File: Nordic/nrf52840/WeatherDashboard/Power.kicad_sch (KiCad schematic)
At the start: 4 parts, among them J1 Conn_01x02_Pin, U1 MPM3805GQB-33-Z

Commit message: pcie connector
Add connectins to the pcie connector
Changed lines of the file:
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@@
+	)
+	(junction
+		(at 156.21 87.63)
+		(diameter 0)
+		(color 0 0 0 0)
 	)
 	(junction
@@
 	(wire
 		(pts
+			(xy 156.21 87.63) (xy 165.1 87.63)
+		)
+		(stroke
+			(width 0)
+			(type default)
+		)
+	)
+	(wire
+		(pts
 			(xy 148.59 95.25) (xy 151.13 95.25)
 		)
@@
 		(effects
 			(font
+				(size 1.27 1.27)
+			)
+			(justify left)
+		)
+	)
+	(hierarchical_label "GND"
+		(shape input)
+		(at 165.1 87.63 0)
+		(effects
+			(font

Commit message: Layout
layout update
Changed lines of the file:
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@@
 	)
 	(junction
-		(at 120.65 87.63)
+		(at 167.64 97.79)
+		(diameter 0)
+		(color 0 0 0 0)
+	)
+	(junction
+		(at 129.54 87.63)
 		(diameter 0)
 		(color 0 0 0 0)
@@
 	(wire
 		(pts
-			(xy 156.21 97.79) (xy 170.18 97.79)
+			(xy 156.21 97.79) (xy 167.64 97.79)
 		)
 		(stroke
@@
 	(wire
 		(pts
-			(xy 129.54 85.09) (xy 120.65 85.09)
-		)
-		(stroke
-			(width 0)
-			(type default)
-		)
-	)
-	(wire
-		(pts
 			(xy 120.65 105.41) (xy 120.65 107.95)
 		)
@@
 	(wire
 		(pts
-			(xy 120.65 87.63) (xy 129.54 87.63)
+			(xy 167.64 97.79) (xy 170.18 97.79)
 		)
 		(stroke
@@
 	(wire
 		(pts
+			(xy 121.92 87.63) (xy 129.54 87.63)
+		)
+		(stroke
+			(width 0)
+			(type default)
+		)
+	)
+	(wire
+		(pts
+			(xy 121.92 88.9) (xy 121.92 87.63)
+		)
+		(stroke
+			(width 0)
+			(type default)
+		)
+	)
+	(wire
+		(pts
 			(xy 120.65 97.79) (xy 129.54 97.79)
 		)
@@
 	(wire
 		(pts
-			(xy 120.65 85.09) (xy 120.65 87.63)
+			(xy 129.54 85.09) (xy 129.54 87.63)
 		)
 		(stroke
@@
 			)
 			(justify left)
+		)
+	)
+	(symbol
+		(lib_id "power:GND")
+		(at 121.92 88.9 0)
+		(unit 1)
+		(exclude_from_sim no)
+		(in_bom yes)
+		(on_board yes)
+		(dnp no)
+		(fields_autoplaced yes)
+		(property "Reference" "#PWR018"
+			(at 121.92 95.25 0)
+			(effects
+				(font
+					(size 1.27 1.27)
+				)
+				(hide yes)
+			)
+		)
+		(property "Value" "GND"
+			(at 121.92 93.98 0)
+			(effects
+				(font
+					(size 1.27 1.27)
+				)
+			)
+		)
+		(property "Footprint" ""
+			(at 121.92 88.9 0)
+			(effects
+				(font
+					(size 1.27 1.27)
+				)
+				(hide yes)
+			)
+		)
+		(property "Datasheet" ""
+			(at 121.92 88.9 0)
+			(effects
+				(font
+					(size 1.27 1.27)
+				)
+				(hide yes)
+			)
+		)
+		(property "Description" "Power symbol creates a global label with name \"GND\" , ground"
+			(at 121.92 88.9 0)
+			(effects
+				(font
+					(size 1.27 1.27)
+				)
+				(hide yes)
+			)
+		)
+		(pin "1"
+		)
+		(instances
+			(project "WeatherDashboard"
+				(path "/189808bb-364f-4c11-a922-cc9d9f33a674/3f611b1e-4b9e-472b-bbce-6aa18c3c2d69"
+					(reference "#PWR018")
+					(unit 1)
+				)
+			)
 		)
 	)
@@
 		(on_board yes)
 		(dnp no)
-		(property "Reference" "#PWR?"
+		(property "Reference" "#PWR0102"
 			(at 156.21 93.98 0)
 			(effects
@@
 			(project "WeatherDashboard"
 				(path "/189808bb-364f-4c11-a922-cc9d9f33a674/3f611b1e-4b9e-472b-bbce-6aa18c3c2d69"
-					(reference "#PWR?")
+					(reference "#PWR0102")
 					(unit 1)
 				)
@@
 	)
 	(symbol
+		(lib_id "power:PWR_FLAG")
+		(at 167.64 97.79 0)
+		(unit 1)
+		(exclude_from_sim no)
+		(in_bom yes)
+		(on_board yes)
+		(dnp no)
+		(fields_autoplaced yes)
+		(property "Reference" "#FLG01"
+			(at 167.64 95.885 0)
+			(effects
+				(font
+					(size 1.27 1.27)
+				)
+				(hide yes)
+			)
+		)
+		(property "Value" "PWR_FLAG"
+			(at 167.64 92.71 0)
+			(effects
+				(font
+					(size 1.27 1.27)
+				)
+			)
+		)
+		(property "Footprint" ""
+			(at 167.64 97.79 0)
+			(effects
+				(font
+					(size 1.27 1.27)
+				)
+				(hide yes)
+			)
+		)
+		(property "Datasheet" "~"
+			(at 167.64 97.79 0)
+			(effects
+				(font
+					(size 1.27 1.27)
+				)
+				(hide yes)
+			)
+		)
+		(property "Description" "Special symbol for telling ERC where power comes from"
+			(at 167.64 97.79 0)
+			(effects
+				(font
+					(size 1.27 1.27)
+				)
+				(hide yes)
+			)
+		)
+		(pin "1"
+		)
+		(instances
+			(project "WeatherDashboard"
+				(path "/189808bb-364f-4c11-a922-cc9d9f33a674/3f611b1e-4b9e-472b-bbce-6aa18c3c2d69"
+					(reference "#FLG01")
+					(unit 1)
+				)
+			)
+		)
+	)
+	(symbol
 		(lib_id "power:GND")
 		(at 167.64 102.87 0)
@@
 	)
 	(symbol
-		(lib_id "power:GND")
-		(at 120.65 87.63 0)
-		(unit 1)
-		(exclude_from_sim no)
-		(in_bom yes)
-		(on_board yes)
-		(dnp no)
-		(fields_autoplaced yes)
-		(property "Reference" "#PWR01"
-			(at 120.65 93.98 0)
-			(effects
-				(font
-					(size 1.27 1.27)
-				)
-				(hide yes)
-			)
-		)
-		(property "Value" "GND"
-			(at 120.65 92.71 0)
-			(effects
-				(font
-					(size 1.27 1.27)
-				)
-			)
-		)
-		(property "Footprint" ""
-			(at 120.65 87.63 0)
-			(effects
-				(font
-					(size 1.27 1.27)
-				)
-				(hide yes)
-			)
-		)
-		(property "Datasheet" ""
-			(at 120.65 87.63 0)
-			(effects
-				(font
-					(size 1.27 1.27)
-				)
-				(hide yes)
-			)
-		)
-		(property "Description" "Power symbol creates a global label with name \"GND\" , ground"
-			(at 120.65 87.63 0)
-			(effects
-				(font
-					(size 1.27 1.27)
-				)
-				(hide yes)
-			)
-		)
-		(pin "1"
-		)
-		(instances
-			(project "WeatherDashboard"
-				(path "/189808bb-364f-4c11-a922-cc9d9f33a674/3f611b1e-4b9e-472b-bbce-6aa18c3c2d69"
-					(reference "#PWR01")
-					(unit 1)
-				)
-			)
-		)
-	)
-	(symbol
 		(lib_id "Connector:Conn_01x02_Pin")
 		(at 175.26 100.33 180)
@@
 		(dnp no)
 		(fields_autoplaced yes)
-		(property "Reference" "#PWR?"
+		(property "Reference" "#PWR0101"
 			(at 153.67 114.3 0)
 			(effects
@@
 			(project "WeatherDashboard"
 				(path "/189808bb-364f-4c11-a922-cc9d9f33a674/3f611b1e-4b9e-472b-bbce-6aa18c3c2d69"
-					(reference "#PWR?")
+					(reference "#PWR0101")
 					(unit 1)
 				)

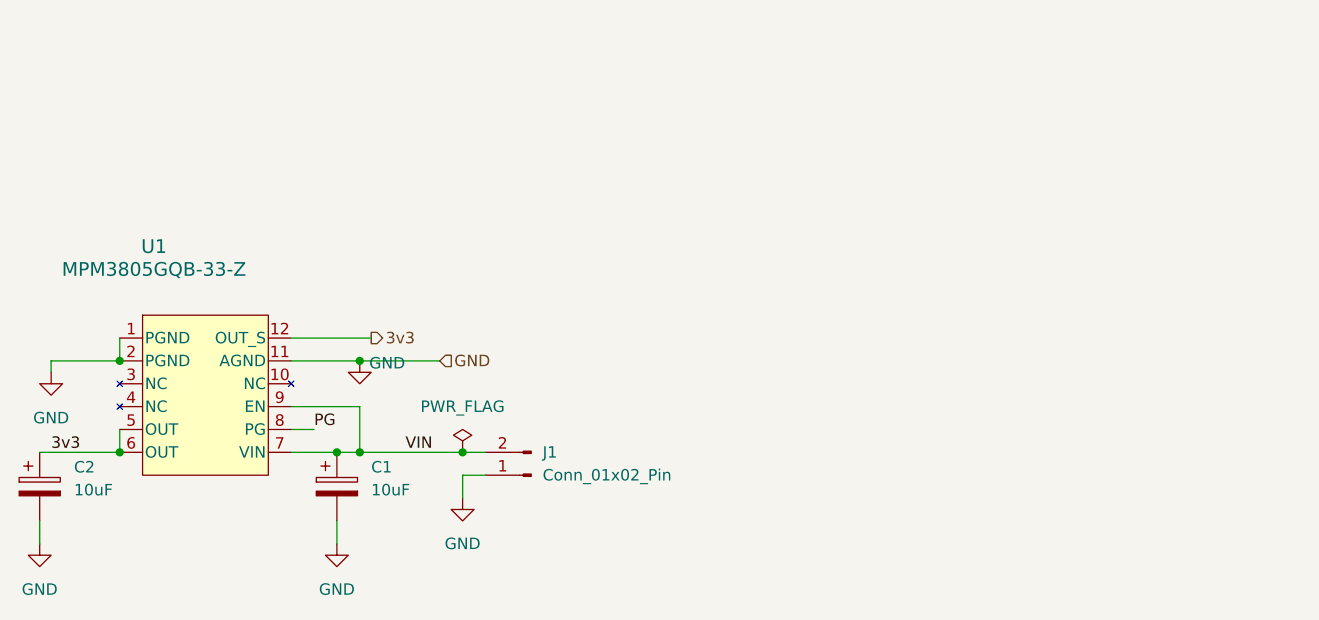
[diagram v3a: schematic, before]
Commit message: layout
Start weather station layout
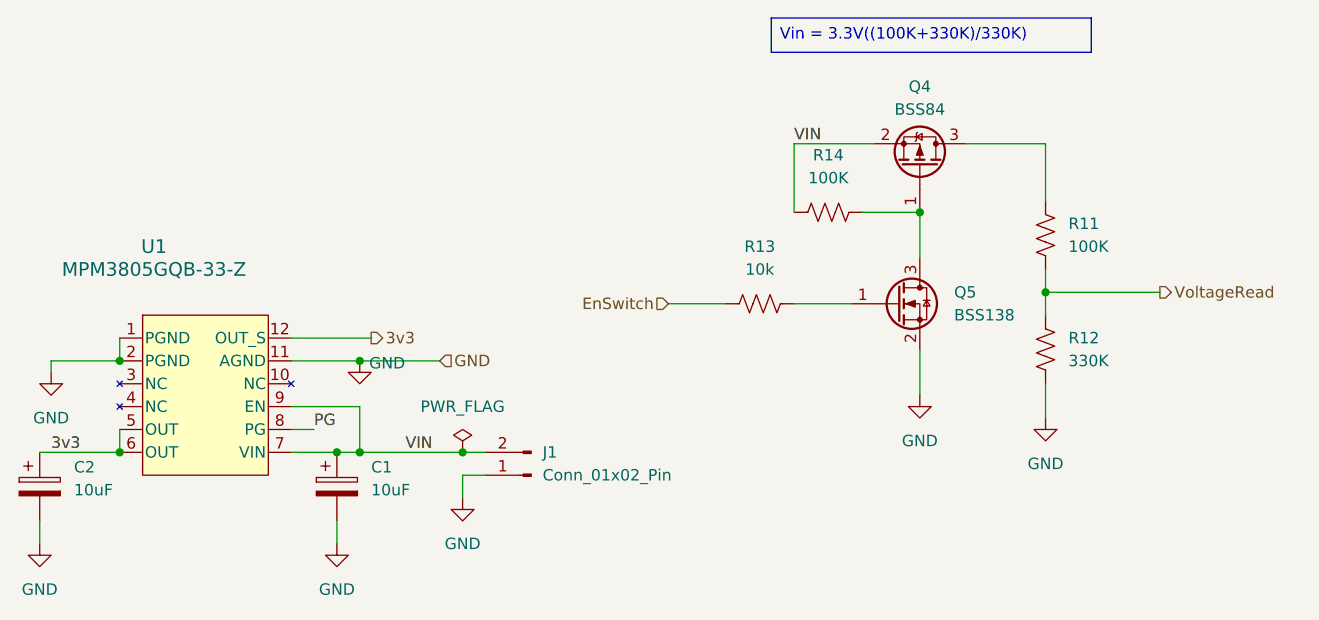
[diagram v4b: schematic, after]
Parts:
- added Q4: BSS84, Package_TO_SOT_SMD:SOT-23, symbol Transistor_FET:BSS84
- added Q5: BSS138, Package_TO_SOT_SMD:SOT-23, symbol Transistor_FET:BSS138
- added R11, R14: 100K, Resistor_SMD:R_0402_1005Metric_Pad0.72x0.64mm_HandSolder, symbol Device:R_US
- added R12: 330K, Resistor_SMD:R_0402_1005Metric_Pad0.72x0.64mm_HandSolder, symbol Device:R_US
- added R13: 10k, Resistor_SMD:R_0402_1005Metric_Pad0.72x0.64mm_HandSolder, symbol Device:R_US
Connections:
- net GND: now also Q5.2 (S), R12.2
- net VIN: now also Q4.2 (S), R14.1
- new net: Q4.1 (G), Q5.3 (D), R14.2
- new net: Q4.3 (D), R11.1
- new net: Q5.1 (G), R13.2
- new net EnSwitch: R13.1
- new net VoltageRead: R11.2, R12.1
